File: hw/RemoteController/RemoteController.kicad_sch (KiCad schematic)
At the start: 64 parts, among them J1 Conn_01x04_Pin, J2 Conn_01x04_Pin, SW2 SW_SPDT, SW3 TC-6610-6*6*8-300g, SW4 TC-6610-6*6*8-300g, SW5 TC-6610-6*6*8-300g, SW6 TC-6610-6*6*8-300g, U1 LM358, U11 LM358, U13 nRF52810-QFxx, U14 LM358, U15 LM358, U2 TPS562200, Y1 32 MHz, Y5 32.768 KHz

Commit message: remote_ctrl: start laying out RF components
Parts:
- C10, C11, C12, C13, C14, C16, C19, C20, C21, C22, C23, C24, C3, C4, C5, C55, C56, C6, C7, C8, C9: footprint Capacitor_SMD:C_0603_1608Metric_Pad1.08x0.95mm_HandSolder -> Capacitor_SMD:C_0402_1005Metric_Pad0.74x0.62mm_HandSolder
- R1, R10, R11, R12, R13, R14, R15, R16, R17, R18, R19, R2, R3, R33, R8, R9: footprint Resistor_SMD:R_0603_1608Metric_Pad0.98x0.95mm_HandSolder -> Resistor_SMD:R_0402_1005Metric_Pad0.72x0.64mm_HandSolder
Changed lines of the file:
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@@
 			)
 		)
-		(property "Footprint" "Resistor_SMD:R_0603_1608Metric_Pad0.98x0.95mm_HandSolder"
+		(property "Footprint" "Resistor_SMD:R_0402_1005Metric_Pad0.72x0.64mm_HandSolder"
 			(at 49.53 122.428 90)
 			(hide yes)
@@
 			)
 		)
-		(property "Footprint" "Capacitor_SMD:C_0603_1608Metric_Pad1.08x0.95mm_HandSolder"
+		(property "Footprint" "Capacitor_SMD:C_0402_1005Metric_Pad0.74x0.62mm_HandSolder"
 			(at 272.0848 40.64 0)
 			(hide yes)
@@
 			)
 		)
-		(property "Footprint" "Resistor_SMD:R_0603_1608Metric_Pad0.98x0.95mm_HandSolder"
+		(property "Footprint" "Resistor_SMD:R_0402_1005Metric_Pad0.72x0.64mm_HandSolder"
 			(at 66.548 125.73 90)
 			(hide yes)
@@
 			)
 		)
-		(property "Footprint" "Capacitor_SMD:C_0603_1608Metric_Pad1.08x0.95mm_HandSolder"
+		(property "Footprint" "Capacitor_SMD:C_0402_1005Metric_Pad0.74x0.62mm_HandSolder"
 			(at 92.71 165.4048 0)
 			(hide yes)
@@
 			)
 		)
-		(property "Footprint" "Resistor_SMD:R_0603_1608Metric_Pad0.98x0.95mm_HandSolder"
+		(property "Footprint" "Resistor_SMD:R_0402_1005Metric_Pad0.72x0.64mm_HandSolder"
 			(at 183.388 113.03 90)
 			(hide yes)
@@
 			)
 		)
-		(property "Footprint" "Capacitor_SMD:C_0603_1608Metric_Pad1.08x0.95mm_HandSolder"
+		(property "Footprint" "Capacitor_SMD:C_0402_1005Metric_Pad0.74x0.62mm_HandSolder"
 			(at 187.96 25.7048 0)
 			(hide yes)
@@
 			)
 		)
-		(property "Footprint" "Resistor_SMD:R_0603_1608Metric_Pad0.98x0.95mm_HandSolder"
+		(property "Footprint" "Resistor_SMD:R_0402_1005Metric_Pad0.72x0.64mm_HandSolder"
 			(at 93.98 84.328 90)
 			(hide yes)
@@
 			)
 		)
-		(property "Footprint" "Capacitor_SMD:C_0603_1608Metric_Pad1.08x0.95mm_HandSolder"
+		(property "Footprint" "Capacitor_SMD:C_0402_1005Metric_Pad0.74x0.62mm_HandSolder"
 			(at 260.0452 66.04 0)
 			(hide yes)
@@
 			)
 		)
-		(property "Footprint" "Capacitor_SMD:C_0603_1608Metric_Pad1.08x0.95mm_HandSolder"
+		(property "Footprint" "Capacitor_SMD:C_0402_1005Metric_Pad0.74x0.62mm_HandSolder"
 			(at 274.32 70.1548 0)
 			(hide yes)
@@
 			)
 		)
-		(property "Footprint" "Capacitor_SMD:C_0603_1608Metric_Pad1.08x0.95mm_HandSolder"
+		(property "Footprint" "Capacitor_SMD:C_0402_1005Metric_Pad0.74x0.62mm_HandSolder"
 			(at 270.2052 66.04 0)
 			(hide yes)
@@
 			)
 		)
-		(property "Footprint" "Capacitor_SMD:C_0603_1608Metric_Pad1.08x0.95mm_HandSolder"
+		(property "Footprint" "Capacitor_SMD:C_0402_1005Metric_Pad0.74x0.62mm_HandSolder"
 			(at 39.0652 87.63 0)
 			(hide yes)
@@
 			)
 		)
-		(property "Footprint" "Resistor_SMD:R_0603_1608Metric_Pad0.98x0.95mm_HandSolder"
+		(property "Footprint" "Resistor_SMD:R_0402_1005Metric_Pad0.72x0.64mm_HandSolder"
 			(at 189.23 99.822 90)
 			(hide yes)
@@
 			)
 		)
-		(property "Footprint" "Resistor_SMD:R_0603_1608Metric_Pad0.98x0.95mm_HandSolder"
+		(property "Footprint" "Resistor_SMD:R_0402_1005Metric_Pad0.72x0.64mm_HandSolder"
 			(at 179.578 113.03 90)
 			(hide yes)
@@
 			)
 		)
-		(property "Footprint" "Resistor_SMD:R_0603_1608Metric_Pad0.98x0.95mm_HandSolder"
+		(property "Footprint" "Resistor_SMD:R_0402_1005Metric_Pad0.72x0.64mm_HandSolder"
 			(at 54.61 147.828 90)
 			(hide yes)
@@
 			)
 		)
-		(property "Footprint" "Capacitor_SMD:C_0603_1608Metric_Pad1.08x0.95mm_HandSolder"
+		(property "Footprint" "Capacitor_SMD:C_0402_1005Metric_Pad0.74x0.62mm_HandSolder"
 			(at 256.8448 40.64 0)
 			(hide yes)
@@
 			)
 		)
-		(property "Footprint" "Capacitor_SMD:C_0603_1608Metric_Pad1.08x0.95mm_HandSolder"
+		(property "Footprint" "Capacitor_SMD:C_0402_1005Metric_Pad0.74x0.62mm_HandSolder"
 			(at 33.02 142.5448 0)
 			(hide yes)
@@
 			)
 		)
-		(property "Footprint" "Capacitor_SMD:C_0603_1608Metric_Pad1.08x0.95mm_HandSolder"
+		(property "Footprint" "Capacitor_SMD:C_0402_1005Metric_Pad0.74x0.62mm_HandSolder"
 			(at 45.4152 87.63 0)
 			(hide yes)
@@
 			)
 		)
-		(property "Footprint" "Resistor_SMD:R_0603_1608Metric_Pad0.98x0.95mm_HandSolder"
+		(property "Footprint" "Resistor_SMD:R_0402_1005Metric_Pad0.72x0.64mm_HandSolder"
 			(at 175.768 113.03 90)
 			(hide yes)
@@
 			)
 		)
-		(property "Footprint" "Capacitor_SMD:C_0603_1608Metric_Pad1.08x0.95mm_HandSolder"
+		(property "Footprint" "Capacitor_SMD:C_0402_1005Metric_Pad0.74x0.62mm_HandSolder"
 			(at 274.32 80.3148 0)
 			(hide yes)
@@
 			)
 		)
-		(property "Footprint" "Capacitor_SMD:C_0603_1608Metric_Pad1.08x0.95mm_HandSolder"
+		(property "Footprint" "Capacitor_SMD:C_0402_1005Metric_Pad0.74x0.62mm_HandSolder"
 			(at 187.96 35.8648 0)
 			(hide yes)
@@
 			)
 		)
-		(property "Footprint" "Resistor_SMD:R_0603_1608Metric_Pad0.98x0.95mm_HandSolder"
+		(property "Footprint" "Resistor_SMD:R_0402_1005Metric_Pad0.72x0.64mm_HandSolder"
 			(at 80.518 90.17 90)
 			(hide yes)
@@
 			)
 		)
-		(property "Footprint" "Resistor_SMD:R_0603_1608Metric_Pad0.98x0.95mm_HandSolder"
+		(property "Footprint" "Resistor_SMD:R_0402_1005Metric_Pad0.72x0.64mm_HandSolder"
 			(at 189.23 102.362 90)
 			(hide yes)
@@
 			)
 		)
-		(property "Footprint" "Capacitor_SMD:C_0603_1608Metric_Pad1.08x0.95mm_HandSolder"
+		(property "Footprint" "Capacitor_SMD:C_0402_1005Metric_Pad0.74x0.62mm_HandSolder"
 			(at 87.63 79.0448 0)
 			(hide yes)
@@
 			)
 		)
-		(property "Footprint" "Resistor_SMD:R_0603_1608Metric_Pad0.98x0.95mm_HandSolder"
+		(property "Footprint" "Resistor_SMD:R_0402_1005Metric_Pad0.72x0.64mm_HandSolder"
 			(at 171.958 113.03 90)
 			(hide yes)
@@
 			)
 		)
-		(property "Footprint" "Capacitor_SMD:C_0603_1608Metric_Pad1.08x0.95mm_HandSolder"
+		(property "Footprint" "Capacitor_SMD:C_0402_1005Metric_Pad0.74x0.62mm_HandSolder"
 			(at 279.7048 40.64 0)
 			(hide yes)
@@
 			)
 		)
-		(property "Footprint" "Resistor_SMD:R_0603_1608Metric_Pad0.98x0.95mm_HandSolder"
+		(property "Footprint" "Resistor_SMD:R_0402_1005Metric_Pad0.72x0.64mm_HandSolder"
 			(at 189.23 94.742 90)
 			(hide yes)
@@
 			)
 		)
-		(property "Footprint" "Capacitor_SMD:C_0603_1608Metric_Pad1.08x0.95mm_HandSolder"
+		(property "Footprint" "Capacitor_SMD:C_0402_1005Metric_Pad0.74x0.62mm_HandSolder"
 			(at 100.0252 93.98 0)
 			(hide yes)
@@
 			)
 		)
-		(property "Footprint" "Capacitor_SMD:C_0603_1608Metric_Pad1.08x0.95mm_HandSolder"
+		(property "Footprint" "Capacitor_SMD:C_0402_1005Metric_Pad0.74x0.62mm_HandSolder"
 			(at 115.57 165.4048 0)
 			(hide yes)
@@
 			)
 		)
-		(property "Footprint" "Capacitor_SMD:C_0603_1608Metric_Pad1.08x0.95mm_HandSolder"
+		(property "Footprint" "Capacitor_SMD:C_0402_1005Metric_Pad0.74x0.62mm_HandSolder"
 			(at 215.9 28.2448 0)
 			(hide yes)
@@
 			)
 		)
-		(property "Footprint" "Capacitor_SMD:C_0603_1608Metric_Pad1.08x0.95mm_HandSolder"
+		(property "Footprint" "Capacitor_SMD:C_0402_1005Metric_Pad0.74x0.62mm_HandSolder"
 			(at 215.9 23.1648 0)
 			(hide yes)
@@
 			)
 		)
-		(property "Footprint" "Resistor_SMD:R_0603_1608Metric_Pad0.98x0.95mm_HandSolder"
+		(property "Footprint" "Resistor_SMD:R_0402_1005Metric_Pad0.72x0.64mm_HandSolder"
 			(at 66.548 116.84 90)
 			(hide yes)
@@
 			)
 		)
-		(property "Footprint" "Resistor_SMD:R_0603_1608Metric_Pad0.98x0.95mm_HandSolder"
+		(property "Footprint" "Resistor_SMD:R_0402_1005Metric_Pad0.72x0.64mm_HandSolder"
 			(at 189.23 97.282 90)
 			(hide yes)
@@
 			)
 		)
-		(property "Footprint" "Capacitor_SMD:C_0603_1608Metric_Pad1.08x0.95mm_HandSolder"
+		(property "Footprint" "Capacitor_SMD:C_0402_1005Metric_Pad0.74x0.62mm_HandSolder"
 			(at 106.3752 93.98 0)
 			(hide yes)
@@
 			)
 		)
-		(property "Footprint" "Resistor_SMD:R_0603_1608Metric_Pad0.98x0.95mm_HandSolder"
+		(property "Footprint" "Resistor_SMD:R_0402_1005Metric_Pad0.72x0.64mm_HandSolder"
 			(at 51.562 83.82 90)
 			(hide yes)
@@
 			)
 		)
-		(property "Footprint" "Capacitor_SMD:C_0603_1608Metric_Pad1.08x0.95mm_HandSolder"
+		(property "Footprint" "Capacitor_SMD:C_0402_1005Metric_Pad0.74x0.62mm_HandSolder"
 			(at 32.7152 87.63 0)
 			(hide yes)
@@
 			)
 		)
-		(property "Footprint" "Resistor_SMD:R_0603_1608Metric_Pad0.98x0.95mm_HandSolder"
+		(property "Footprint" "Resistor_SMD:R_0402_1005Metric_Pad0.72x0.64mm_HandSolder"
 			(at 76.2 133.858 90)
 			(hide yes)
@@
 			)
 		)
-		(property "Footprint" "Capacitor_SMD:C_0603_1608Metric_Pad1.08x0.95mm_HandSolder"
+		(property "Footprint" "Capacitor_SMD:C_0402_1005Metric_Pad0.74x0.62mm_HandSolder"
 			(at 264.4648 40.64 0)
 			(hide yes)

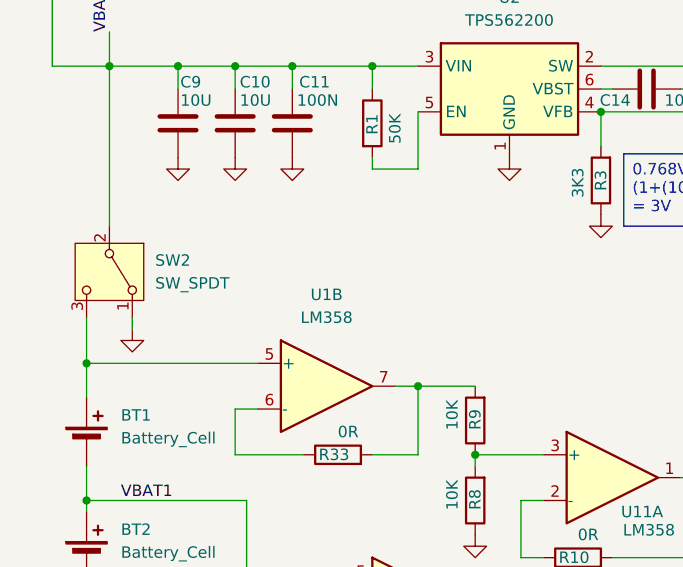
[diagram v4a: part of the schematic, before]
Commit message: remote_ctrl: add RF net class
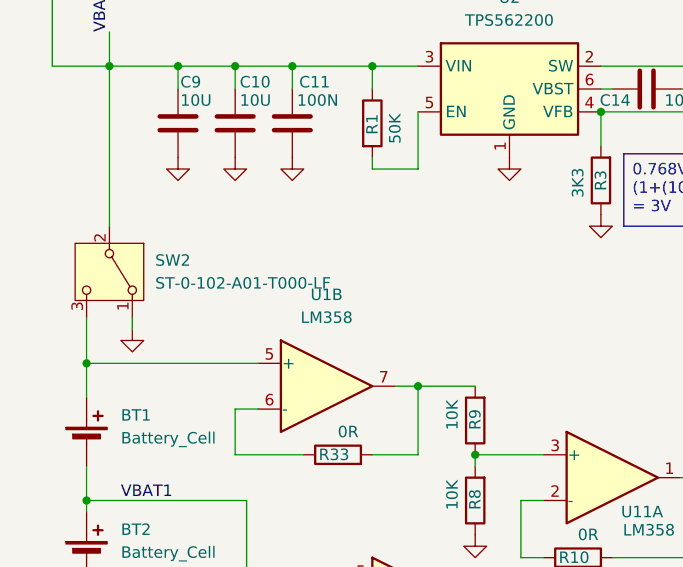
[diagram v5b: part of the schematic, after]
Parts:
- SW2: value SW_SPDT -> ST-0-102-A01-T000-LF; footprint (none) -> Button_Switch_THT:SW_Slide-03_Wuerth-WS-SLTV_10x2.5x6.4_P2.54mm; PN (none) -> ST-0-102-A01-T000-LF
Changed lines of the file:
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@@
 			)
 		)
-		(property "Value" "SW_SPDT"
+		(property "Value" "ST-0-102-A01-T000-LF"
 			(at 29.21 101.5999 90)
 			(show_name no)
@@
 			)
 		)
-		(property "Footprint" ""
+		(property "Footprint" "Button_Switch_THT:SW_Slide-03_Wuerth-WS-SLTV_10x2.5x6.4_P2.54mm"
 			(at 24.13 100.33 0)
 			(hide yes)
@@
 			(hide yes)
 			(show_name no)
+			(do_not_autoplace no)
+			(effects
+				(font
+					(size 1.27 1.27)
+				)
+			)
+		)
+		(property "PN" "ST-0-102-A01-T000-LF"
+			(at 24.13 100.33 90)
+			(hide yes)
+			(show_name no)

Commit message: remote_ctrl: continue placemen
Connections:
- net ~{RX_SHDN}: now reaches U13.16 (P0.13)
- net RX_RSSI: now reaches U13.40 (P0.28/AIN4)
- net AGCDIS renamed RX_SQUELCH
- net IRSEL renamed RX_BW_SEL1
- net PDOUT renamed RX_BW_SEL0
- net RXEN renamed RF_SEL0
- net ~{TXEN} renamed RF_SEL1
- no-connect marks 7 -> 5
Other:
- sheet Radio ports: added RF_SEL0, RF_SEL1, RX_BW_SEL0, RX_BW_SEL1, RX_RSSI, RX_SQUELCH, ~{RX_SHDN}; removed AGCDIS, IRSEL, PDOUT, RXEN, ~{TXEN}

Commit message: remote_ctrl: finish placement
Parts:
- removed SW3, SW4, SW5: TC-6610-6*6*8-300g, Button_Switch_THT:SW_TH_Tactile_Omron_B3F-106x, symbol Switch:SW_Push
- added SW7, SW8, SW9: TS-1088-AR02016, Button_Switch_SMD:SW_SPST_TS-1088-xR020, symbol Switch:SW_Push
- SW6: value TC-6610-6*6*8-300g -> TS-1088-AR02016; footprint Button_Switch_THT:SW_TH_Tactile_Omron_B3F-106x -> Button_Switch_SMD:SW_SPST_TS-1088-xR020
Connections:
- net +3V0: now also SW7.1, SW8.1, SW9.1
- net at R12.2, R18.2: now also SW8.2
- net at R13.2, R17.2: now also SW7.2
- net at R15.2, R19.2: now also SW9.2

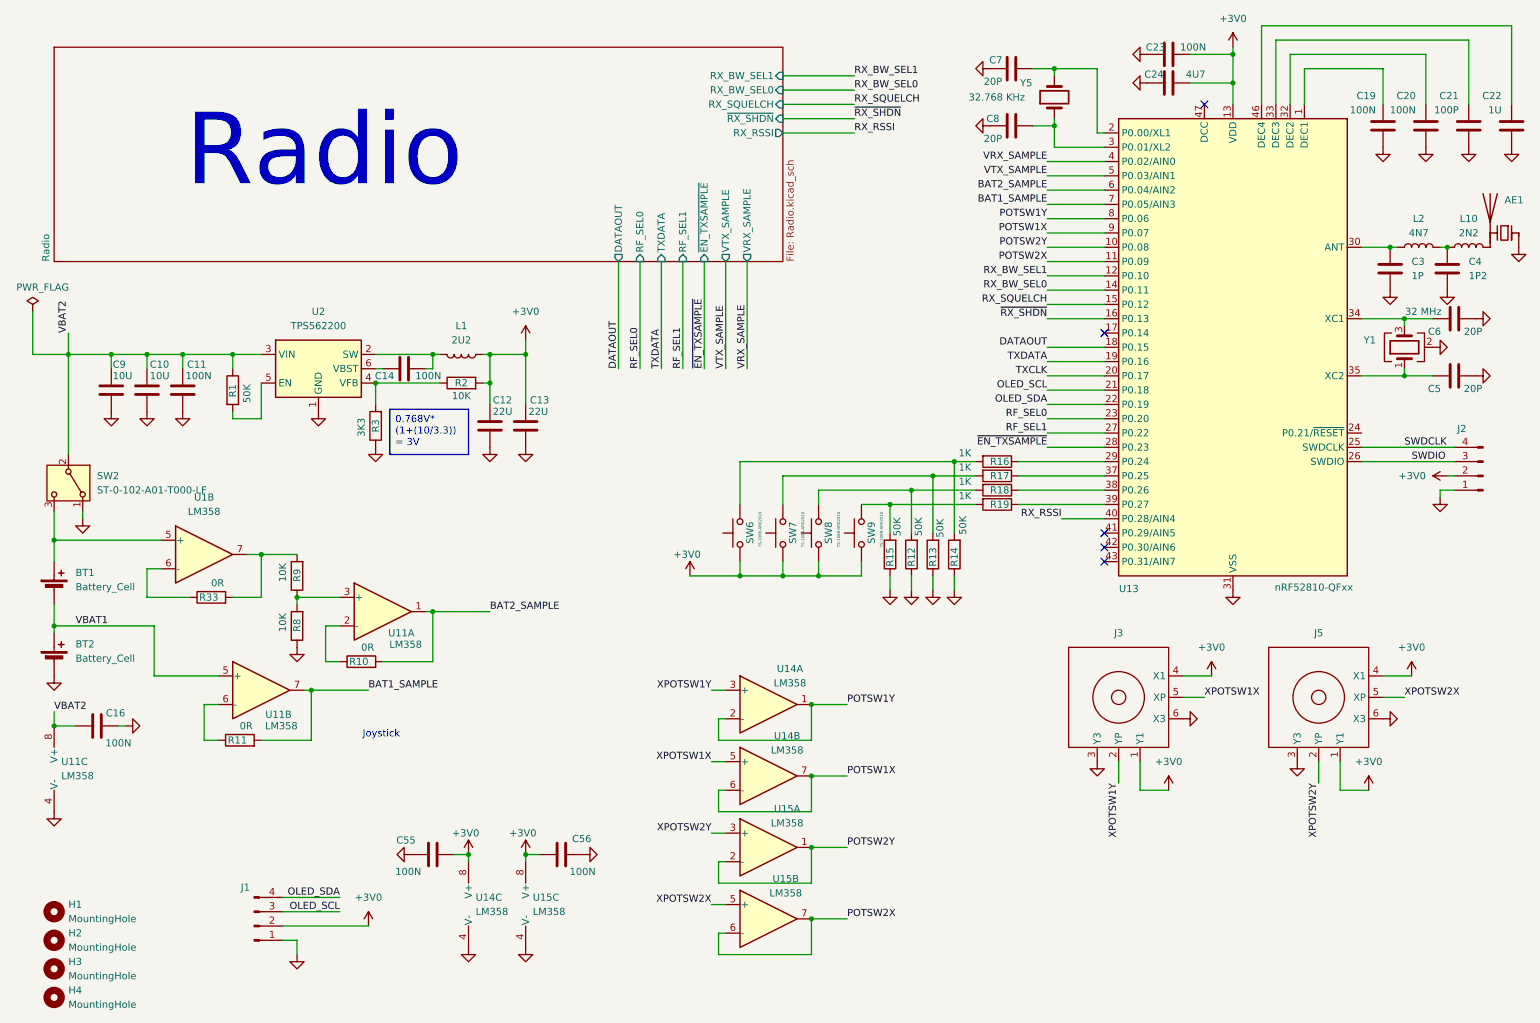
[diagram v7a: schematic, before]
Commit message: remote_ctrl: fix some schematic issues, add battery PTC
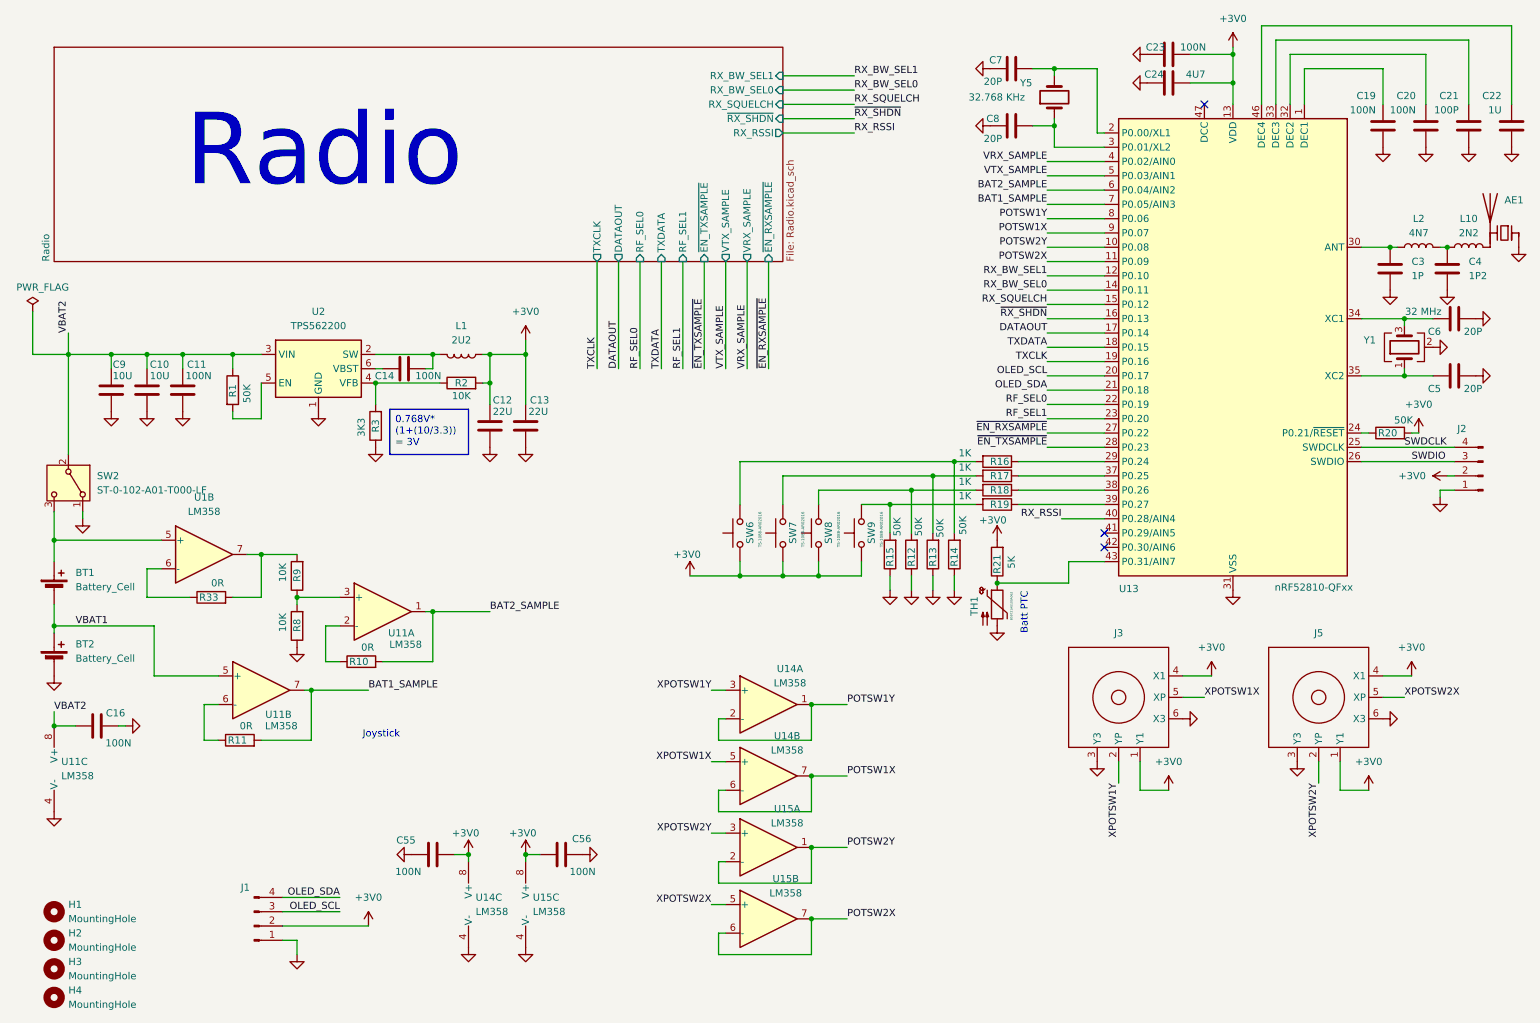
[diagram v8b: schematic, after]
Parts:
- added R20: 50K, Resistor_SMD:R_0402_1005Metric_Pad0.72x0.64mm_HandSolder, symbol Device:R
- added R21: 5K, Resistor_SMD:R_0402_1005Metric_Pad0.72x0.64mm_HandSolder, symbol Device:R
- added TH1: B59721A0100A062, Resistor_SMD:R_0805_2012Metric_Pad1.20x1.40mm_HandSolder, symbol Device:Thermistor_PTC
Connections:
- net +3V0: now also R20.2, R21.2
- net DATAOUT: now also U13.17 (P0.14); no longer U13.18 (P0.15)
- net GND: now also TH1.2
- net OLED_SCL: now also U13.20 (P0.17); no longer U13.21 (P0.18)
- net OLED_SDA: now also U13.21 (P0.18); no longer U13.22 (P0.19)
- net RF_SEL0: now also U13.22 (P0.19); no longer U13.23 (P0.20)
- net RF_SEL1: now also U13.23 (P0.20); no longer U13.27 (P0.22)
- net TXCLK: now also U13.19 (P0.16); no longer U13.20 (P0.17)
- net TXDATA: now also U13.18 (P0.15); no longer U13.19 (P0.16)
- net at U13.24 (P0.21/~{RESET}): now also R20.1
- net at U13.43 (P0.31/AIN7): now also R21.1, TH1.1
- new net ~{EN_RXSAMPLE}: U13.27 (P0.22)
- no-connect marks 5 -> 3
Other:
- sheet Radio ports: added TXCLK, ~{EN_RXSAMPLE}; removed none
- note added: "Batt PTC"
